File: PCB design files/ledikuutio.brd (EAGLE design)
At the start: 118.7 x 69.5 mm, 71 parts, among them IC1 ATMEGA328P, IC2 ISO7221A, IC3 74HC595D, Q2 MOSFET-NCHANNELSMD, Q3 16mhz, T1 TIP42, T2 TIP42, T3 TIP42, T4 TIP42, T5 TIP42, T6 TIP42, T7 TIP42, T8 TIP42, X1 2516-, X2 5566-20, X3 2516-, X4 2516-, X5 2516-, X6 2510-, X7 ANALOG IO

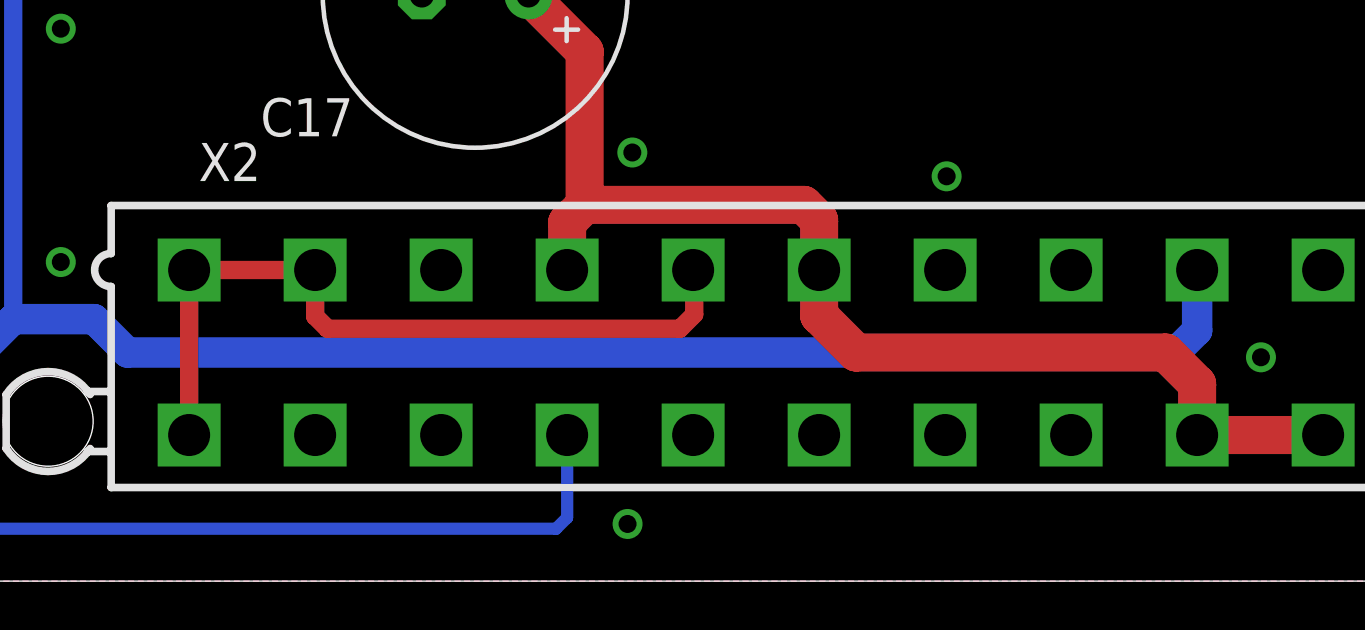
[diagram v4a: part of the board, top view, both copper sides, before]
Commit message: Fix schematic. 3.3V rail was connected to GND.
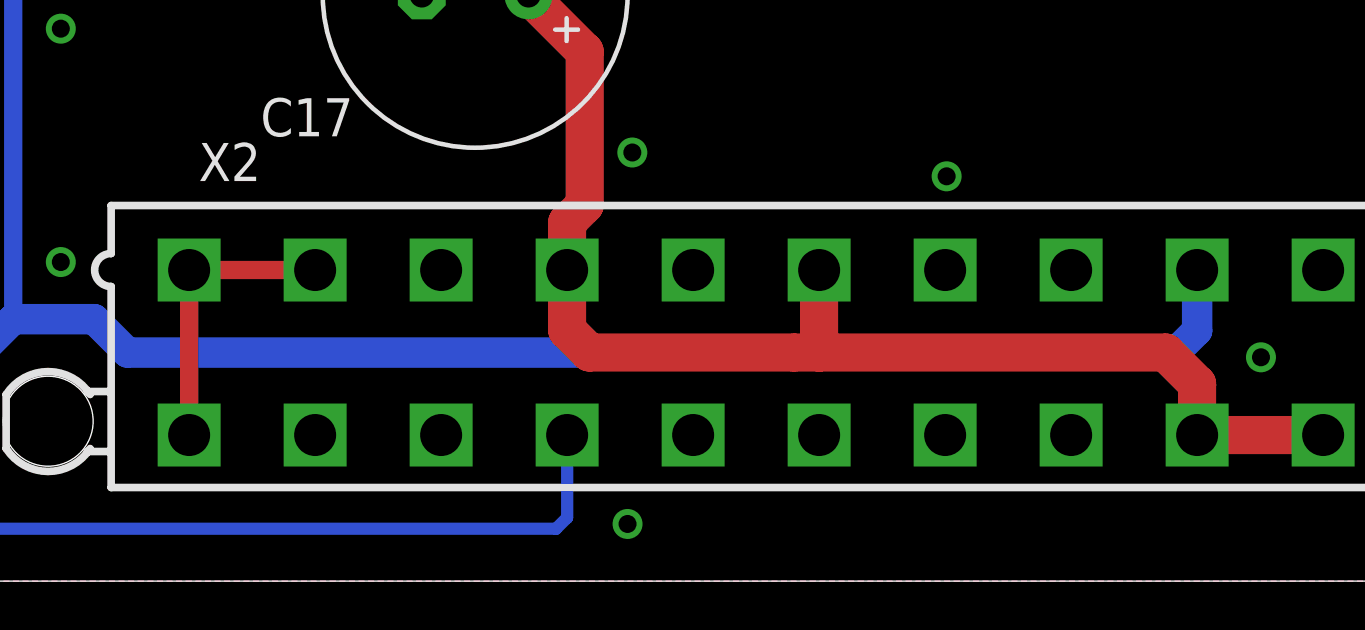
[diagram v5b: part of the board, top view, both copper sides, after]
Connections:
- net +3V3: no longer X2.5
- net GND: now also X2.5
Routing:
- net +3V3: track 25.7 -> 9.70 mm
- net +5V: track 266.7 -> 268.5 mm
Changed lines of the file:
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@@
 <layer number="23" name="tOrigins" color="15" fill="1" visible="yes" active="yes"/>
 <layer number="24" name="bOrigins" color="15" fill="1" visible="yes" active="yes"/>
-<layer number="25" name="tNames" color="7" fill="1" visible="no" active="yes"/>
-<layer number="26" name="bNames" color="7" fill="1" visible="no" active="yes"/>
+<layer number="25" name="tNames" color="7" fill="1" visible="yes" active="yes"/>
+<layer number="26" name="bNames" color="7" fill="1" visible="yes" active="yes"/>
 <layer number="27" name="tValues" color="7" fill="1" visible="no" active="yes"/>
 <layer number="28" name="bValues" color="7" fill="1" visible="no" active="yes"/>
@@
 <via x="46.83125" y="20.955" extent="1-16" drill="0.6" diameter="0.8"/>
 <via x="47.9425" y="23.33625" extent="1-16" drill="0.6" diameter="0.8"/>
+<contactref element="X2" pad="5"/>
 </signal>
 <signal name="MOSI" class="1">
@@
 <wire x1="60.0075" y1="43.815" x2="60.0075" y2="43.65375" width="0.4064" layer="1"/>
 <wire x1="103.9175" y1="4.87" x2="108.1175" y2="4.87" width="1.27" layer="1"/>
-<wire x1="91.3175" y1="10.37" x2="91.3175" y2="8.85375" width="1.27" layer="1"/>
-<wire x1="91.3175" y1="8.85375" x2="92.55125" y2="7.62" width="1.27" layer="1"/>
-<wire x1="92.55125" y1="7.62" x2="102.87" y2="7.62" width="1.27" layer="1"/>
+<wire x1="83.66125" y1="7.62" x2="90.4875" y2="7.62" width="1.27" layer="1"/>
+<wire x1="91.3175" y1="7.62" x2="102.87" y2="7.62" width="1.27" layer="1"/>
 <wire x1="102.87" y1="7.62" x2="103.9175" y2="6.5725" width="1.27" layer="1"/>
 <wire x1="103.9175" y1="6.5725" x2="103.9175" y2="4.87" width="1.27" layer="1"/>
-<wire x1="91.3175" y1="10.37" x2="91.3175" y2="12.02875" width="1.27" layer="1"/>
-<wire x1="91.3175" y1="12.02875" x2="90.805" y2="12.54125" width="1.27" layer="1"/>
-<wire x1="90.805" y1="12.54125" x2="83.5025" y2="12.54125" width="1.27" layer="1"/>
 <wire x1="83.5025" y1="12.54125" x2="82.9175" y2="11.95625" width="1.27" layer="1"/>
 <wire x1="82.9175" y1="11.95625" x2="82.9175" y2="10.37" width="1.27" layer="1"/>
@@
 <wire x1="101.75875" y1="26.6725" x2="102.07875" y2="26.3525" width="0.8128" layer="1"/>
 <wire x1="62.865" y1="38.89375" x2="61.53785" y2="38.89375" width="0.4064" layer="1"/>
+<wire x1="83.66125" y1="7.62" x2="82.9175" y2="8.36375" width="1.27" layer="1"/>
+<wire x1="82.9175" y1="8.36375" x2="82.9175" y2="10.37" width="1.27" layer="1"/>
+<wire x1="91.3175" y1="10.37" x2="91.3175" y2="7.62" width="1.27" layer="1"/>
+<wire x1="91.3175" y1="7.62" x2="90.4875" y2="7.62" width="1.27" layer="1"/>
 </signal>
 <signal name="PS_ON" class="1">
@@
 <contactref element="X2" pad="1"/>
 <contactref element="X2" pad="2"/>
-<contactref element="X2" pad="5"/>
-<wire x1="87.1175" y1="10.37" x2="87.15375" y2="10.33375" width="0.6096" layer="1"/>
-<wire x1="87.15375" y1="10.33375" x2="87.15375" y2="8.89" width="0.6096" layer="1"/>
-<wire x1="87.15375" y1="8.89" x2="86.6775" y2="8.41375" width="0.6096" layer="1"/>
-<wire x1="86.6775" y1="8.41375" x2="74.93" y2="8.41375" width="0.6096" layer="1"/>
-<wire x1="74.93" y1="8.41375" x2="74.5175" y2="8.82625" width="0.6096" layer="1"/>
-<wire x1="74.5175" y1="8.82625" x2="74.5175" y2="10.37" width="0.6096" layer="1"/>
 <wire x1="74.5175" y1="10.37" x2="70.3175" y2="10.37" width="0.6096" layer="1"/>
-<wire x1="70.3175" y1="4.87" x2="70.3175" y2="10.37" width="0.6096" layer="1"/>
+<wire x1="70.3175" y1="10.37" x2="70.3175" y2="4.87" width="0.6096" layer="1"/>
 </signal>
 <signal name="TXD_FT232R">

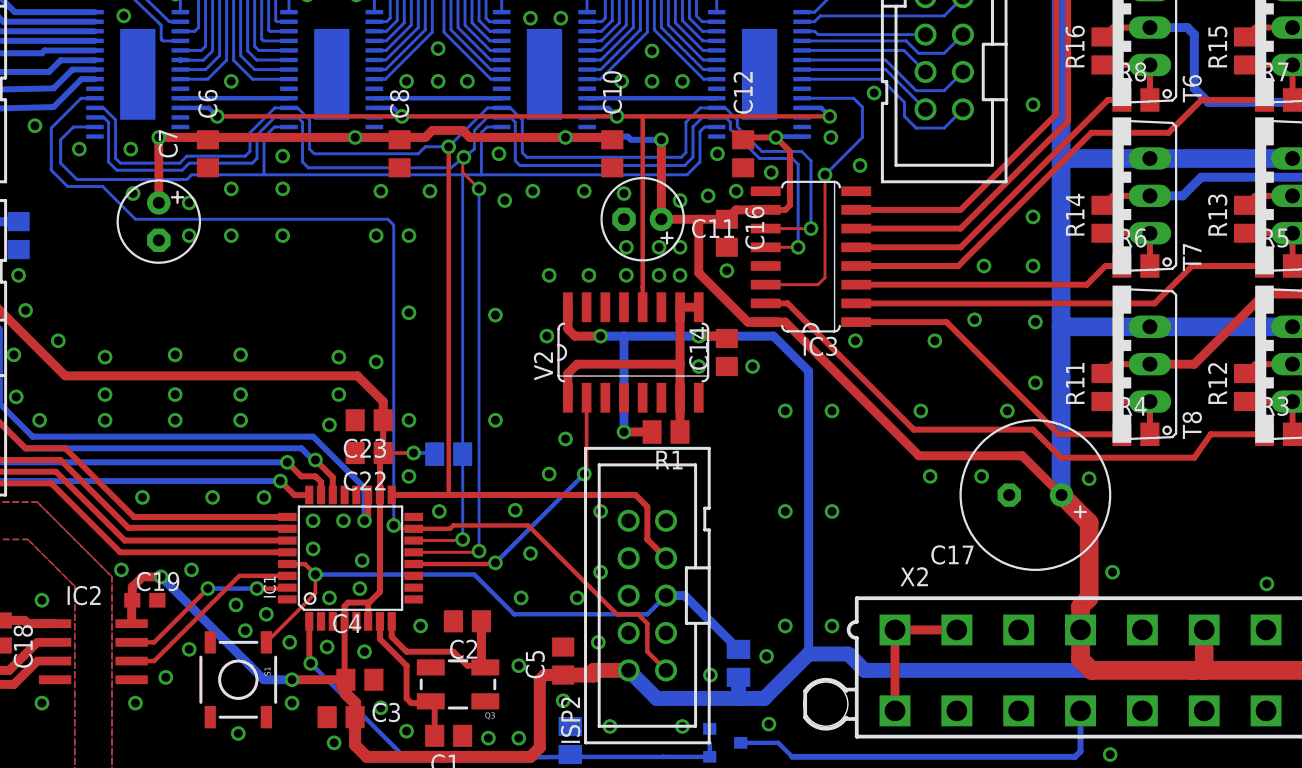
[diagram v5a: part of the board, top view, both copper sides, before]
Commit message: Add missing IREF resistors.
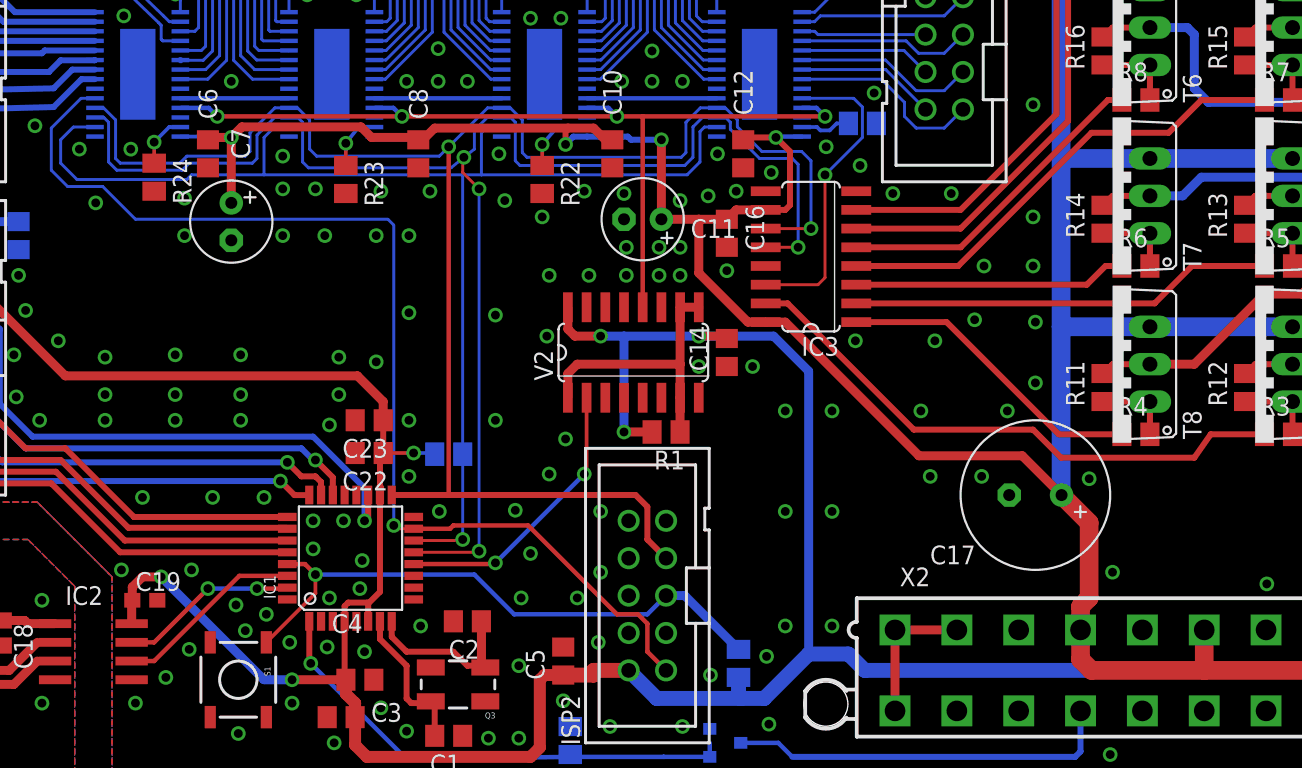
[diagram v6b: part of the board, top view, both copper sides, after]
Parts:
- added R21, R22, R23, R24: 1920ohm, rcl:M0805
- moved C7 4.92 mm to (25.2, 38.1)
- moved C8 1.27 mm to (37.9, 42.7)
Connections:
- new net N$48: R24.1, U$1.27
- new net N$5: R21.1, U$4.27
- new net N$6: R23.1, U$2.27
- new net N$99: R22.1, U$3.27
- net GND: now also R21.2, R22.2, R23.2, R24.2
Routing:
- net N$99: track 0.00 -> 5.02 mm, vias 0 -> 1
- net N$6: track 0.00 -> 3.99 mm, vias 0 -> 1
- net N$48: track 0.00 -> 3.64 mm, vias 0 -> 1
- net N$5: track 0.00 -> 3.44 mm
- net +5V: track 268.5 -> 270.0 mm, vias 5 -> 4
- net GSCLK/4: track 63.8 -> 63.2 mm

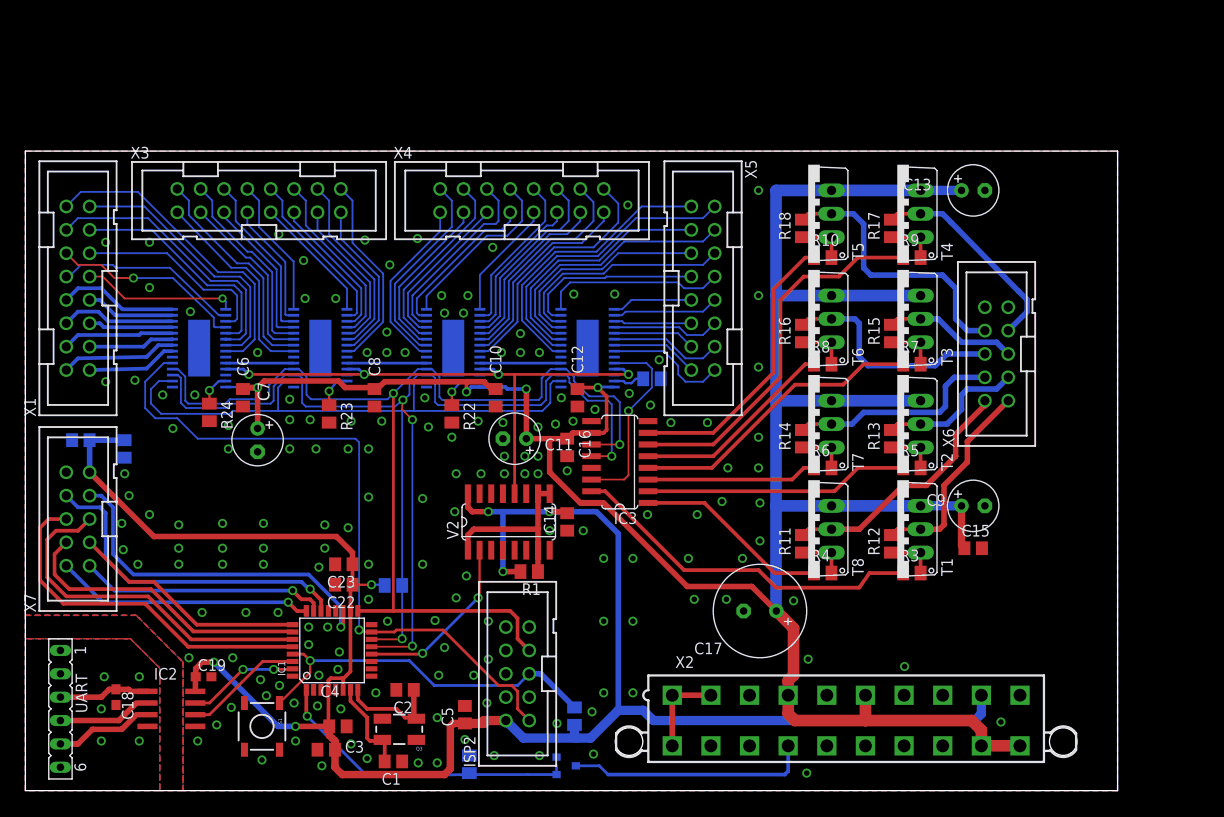
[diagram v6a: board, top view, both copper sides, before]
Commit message: Tweak drill sizes and add tip42C to local library.
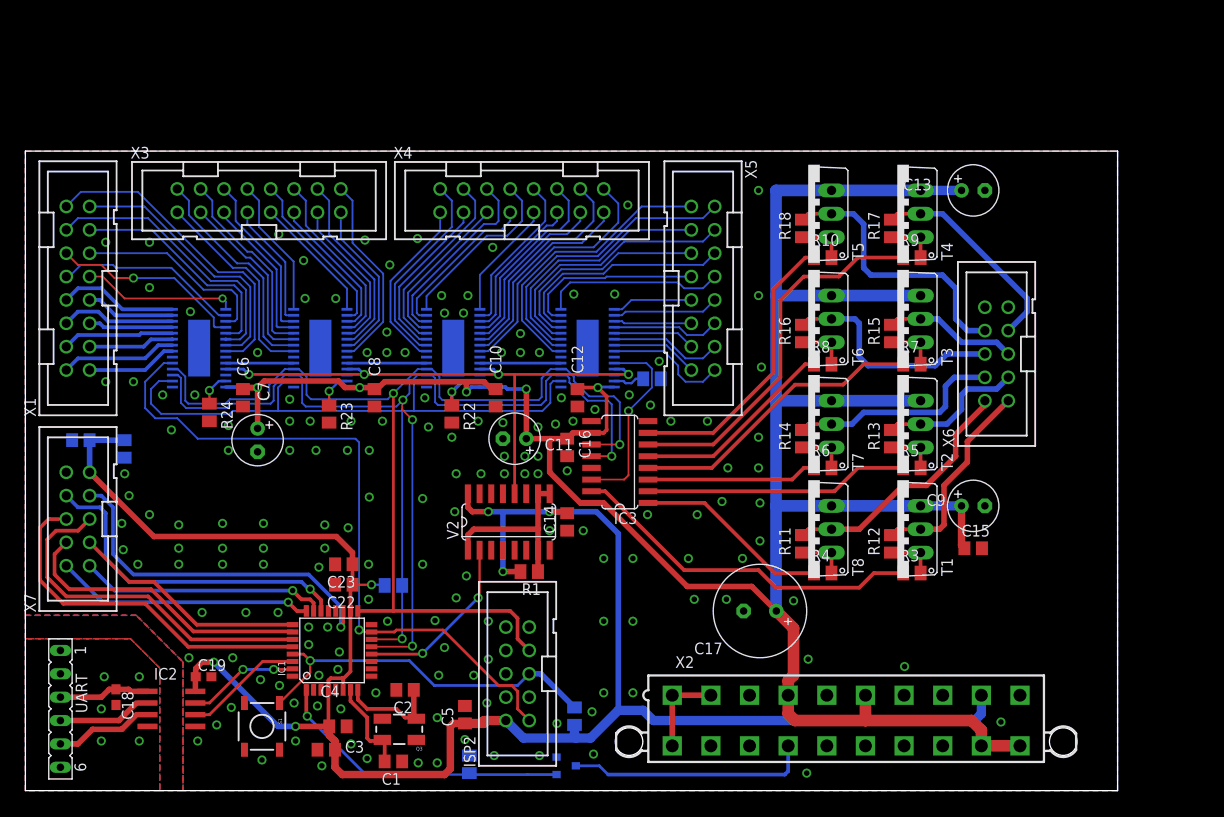
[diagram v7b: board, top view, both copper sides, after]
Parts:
- T1, T7: device transistor-power:TO220AV -> elovalo:TO220AV
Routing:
- net +5V: track 270.0 -> 271.4 mm, vias 4 -> 5
- net PS_ON: track 33.8 -> 32.8 mm
